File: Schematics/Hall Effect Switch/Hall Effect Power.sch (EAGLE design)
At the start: 8 parts, among them IC1 A1203LH, Q1 PH7030L

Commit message: Misc Routing
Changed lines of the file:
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@@
 <wire x1="45.72" y1="30.48" x2="45.72" y2="22.86" width="0.1524" layer="91"/>
 <wire x1="45.72" y1="22.86" x2="86.36" y2="22.86" width="0.1524" layer="91"/>
-<label x="88.9" y="40.64" size="1.778" layer="95"/>
+<label x="88.9" y="48.26" size="1.778" layer="95"/>
 </segment>
 </net>
@@
 <wire x1="45.72" y1="48.26" x2="68.58" y2="48.26" width="0.1524" layer="91"/>
 <wire x1="68.58" y1="48.26" x2="68.58" y2="40.64" width="0.1524" layer="91"/>
-<label x="35.56" y="48.26" size="1.778" layer="95"/>
+<label x="40.64" y="48.26" size="1.778" layer="95"/>
 </segment>
 </net>

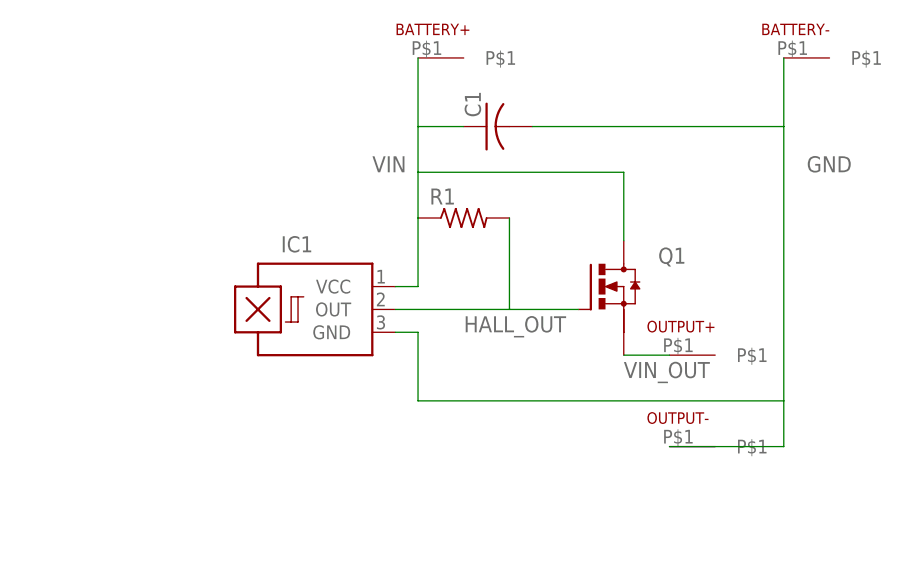
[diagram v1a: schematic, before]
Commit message: New Hall Effect Switch
Changed all the parts for the hall effect switch.
The goal is lower passive power consumption and lower Rds(on).

Panelized the new hall effect switch.
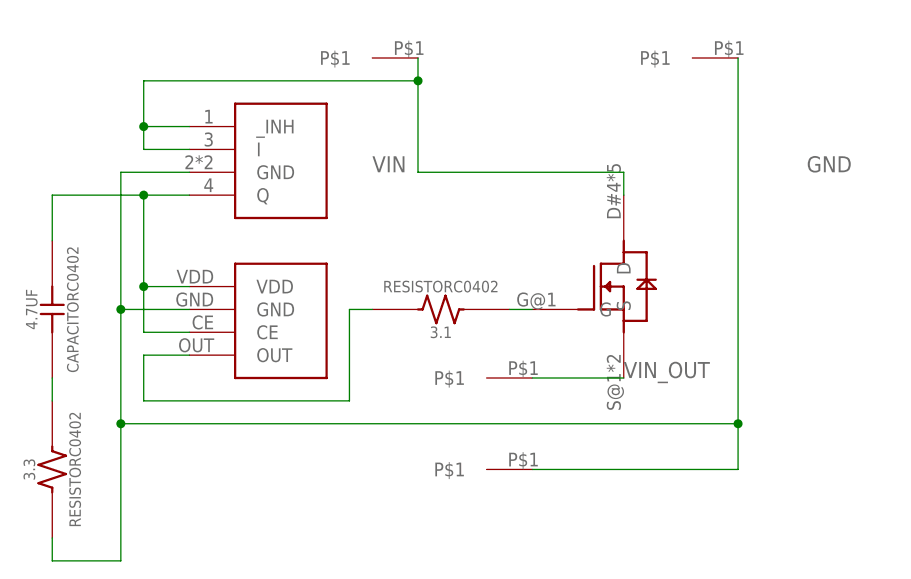
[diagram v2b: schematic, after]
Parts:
- removed BATTERY+, BATTERY-, OUTPUT+, OUTPUT-: SINGLE_WIRE, ROCKET CLUB:SINGLE_WIRE
- removed C1: (no value), rcl:C-USC1206
- removed IC1: A1203LH, allegro:A1203LH
- removed Q1: PH7030L, transistor-power:PH7030L
- removed R1: (no value), resistor:R-US_R1206
- added 3.1, 3.3: RESISTORC0402, RocketControlBoard:RESISTORC0402
- added 4.7UF: CAPACITORC0402, RocketControlBoard:CAPACITORC0402
- added U$1: HALL-MOSFET-NEW, RocketControlBoard:HALL-MOSFET-NEW
- added U$2: HALL-HALL-NEW, RocketControlBoard:HALL-HALL-NEW
- added U$3: HALL-REG-NEW, RocketControlBoard:HALL-REG-NEW
- added U$4, U$5, U$6, U$7: SINGLE-WIRE, RocketControlBoard:SINGLE-WIRE
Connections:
- new net N$1: 4.7UF.B, U$2.CE, U$2.VDD, U$3.Q
- new net N$2: 3.3.P$2, 4.7UF.A
- new net N$3: 3.1.P$1, U$1.G
- net GND: now also 3.3.P$1, U$2.GND, U$3.GND, U$4.P$1, U$7.P$1; no longer BATTERY-.P$1, C1.2, IC1.GND, OUTPUT-.P$1
- net HALL_OUT: now also 3.1.P$2, U$2.OUT; no longer IC1.OUT, Q1.G, R1.2
- net VIN: now also U$1.D, U$3.I, U$3._INH, U$6.P$1; no longer BATTERY+.P$1, C1.1, IC1.VCC, Q1.D, R1.1
- net VIN_OUT: now also U$1.S, U$5.P$1; no longer OUTPUT+.P$1, Q1.S
